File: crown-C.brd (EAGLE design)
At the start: 302 x 51.5 mm, 15 parts

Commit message: Mostly routed! :D
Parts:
- added U$1, U$3, U$4, U$5, U$6, U$7, U$8, U$9: SMD_BREADBOARD, pcb_crown:SMD_BREADBOARD_4X
- added U$10, U$11, U$12, U$13, U$14, U$15, U$16, U$17, U$18, U$19, U$20, U$21, U$22, U$23, U$24, U$25, U$26, U$27, U$28, U$29, U$30, U$31, U$32, U$33, U$34, U$35, U$36, U$37, U$38, U$39, U$40, U$41, U$42, U$43, U$44, U$45, U$46, U$47, U$48, U$49, U$50, U$51, U$52, U$53, U$54, U$55, U$56, U$57, U$58, U$59, U$60, U$61, U$62, U$63, U$64, U$65, U$66, U$67, U$68, U$69, U$70, U$71: SMD_PAD, pcb_crown:SMD_BREADBOARD_PAD
- moved SKIP-PTH1 10.0 mm to (19.6, 51.6), turned to 90 degrees
- moved C3 9.34 mm to (38.9, 53.8), turned to 270 degrees
- moved C4 9.24 mm to (19.8, 47.5), turned to 90 degrees
- moved SKIP-PTH2 4.64 mm to (49.3, 59.7)
- moved PTH1 0.13 mm to (14.5, 58.4)
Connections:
- net PTH-DI renamed PB1
- net SMD-DI renamed PB0
- new net A0: U$2.P$13, U$2.P$32, U$44.P$1, U$55.P$1
- new net A1: U$2.P$14, U$2.P$33, U$43.P$1, U$56.P$1
- new net A2: U$2.P$15, U$2.P$34, U$42.P$1, U$58.P$1
- new net N$11: U$14.P$1, U$15.P$1, U$5.P$3, U$57.P$1
- new net N$12: U$12.P$1, U$13.P$1, U$50.P$1, U$6.P$3
- new net N$13: U$10.P$1, U$11.P$1, U$49.P$1, U$7.P$3
- new net N$14: U$40.P$1, U$41.P$1, U$7.P$7, U$71.P$1
- new net N$15: U$38.P$1, U$39.P$1, U$6.P$7, U$70.P$1
- new net N$16: U$36.P$1, U$37.P$1, U$5.P$7, U$69.P$1
- new net N$17: U$34.P$1, U$35.P$1, U$4.P$7, U$68.P$1
- new net N$18: U$32.P$1, U$33.P$1, U$67.P$1, U$8.P$7
- new net N$19: U$30.P$1, U$31.P$1, U$66.P$1, U$9.P$7
- new net N$2: U$1.P$3, U$24.P$1, U$25.P$1, U$63.P$1
- new net N$20: U$28.P$1, U$29.P$1, U$3.P$7, U$65.P$1
- new net N$21: U$1.P$7, U$26.P$1, U$27.P$1, U$64.P$1
- new net N$6: U$22.P$1, U$23.P$1, U$3.P$3, U$62.P$1
- new net N$7: U$20.P$1, U$21.P$1, U$61.P$1, U$9.P$3
- new net N$8: U$18.P$1, U$19.P$1, U$60.P$1, U$8.P$3
- new net N$9: U$16.P$1, U$17.P$1, U$4.P$3, U$59.P$1
- new net PB2: U$2.P$28, U$2.P$9, U$48.P$1, U$51.P$1
- new net PB3: U$2.P$10, U$2.P$29, U$47.P$1, U$52.P$1
- new net PB4: U$2.P$11, U$2.P$30, U$46.P$1, U$53.P$1
- new net PB5: U$2.P$12, U$2.P$31, U$45.P$1, U$54.P$1
- net GND: now also U$1.P$2, U$2.P$18, U$2.P$37, U$3.P$2, U$4.P$2, U$5.P$2, U$6.P$2, U$7.P$2, U$8.P$2, U$9.P$2
- net N$4: now also U$2.P$19
- net PTH-DO: now also U$2.P$38
- net VBAT: now also U$2.P$16, U$2.P$35
- net VLIVE: now also U$1.P$1, U$2.P$17, U$2.P$36, U$3.P$1, U$4.P$1, U$5.P$1, U$6.P$1, U$7.P$1, U$8.P$1, U$9.P$1
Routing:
- net A2: track 0.00 -> 111.5 mm
- net A1: track 0.00 -> 108.2 mm
- net A0: track 0.00 -> 103.5 mm
- net PB5: track 0.00 -> 102.3 mm
- net PB4: track 0.00 -> 99.6 mm
- net PB3: track 0.00 -> 96.8 mm
- net PB2: track 0.00 -> 93.7 mm
- net VBAT: track 109.0 -> 194.9 mm
- net VLIVE: track 179.6 -> 240.0 mm, vias 7 -> 5
- net GND: track 172.9 -> 217.8 mm, vias 7 -> 5
- net N$4: track 44.6 -> 66.6 mm
- net N$5: track 67.8 -> 47.4 mm
- net PTH-DO: track 48.9 -> 58.2 mm
- net N$9: track 0.00 -> 7.62 mm
- net N$8: track 0.00 -> 7.62 mm
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- added copper zone on layer 1, net GND
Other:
- board size 302 x 51.5 mm -> 117.3 x 51.5 mm
- board text added: "A0"
- board text added: "A1"
- board text added: "A2"
- board text added: "D10"
- board text added: "D11"
- board text added: "D12"
- board text added: "D13"
- board text added: "SPI"

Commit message: Just cleanup stuff
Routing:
- net VBAT: track 194.9 -> 261.3 mm, vias 1 -> 3
- net VLIVE: track 240.0 -> 290.4 mm, vias 5 -> 6
- net A2: track 111.5 -> 114.6 mm
- net GND: track 217.8 -> 215.3 mm
- net A1: track 108.2 -> 110.7 mm
- net A0: track 103.5 -> 105.5 mm
- net PB5: track 102.3 -> 103.9 mm
- net PB4: track 99.6 -> 100.6 mm
- net PB3: track 96.8 -> 97.3 mm
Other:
- board text added: "A4"
- board text added: "A5"
- board text added: "D3"
- board text added: "D4"
- board text added: "D5"
- board text added: "I2C"
- board text added: "RXI"
- board text added: "TXO"
- board text removed: "A0"
- board text removed: "A1"
- board text removed: "A2"
- board text removed: "D10"
- board text removed: "D11"
- board text removed: "D12"
- board text removed: "D13"
- board text removed: "SPI"

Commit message: tidied up a little bit
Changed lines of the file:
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@@
 <layer number="27" name="tValues" color="7" fill="1" visible="no" active="yes"/>
 <layer number="28" name="bValues" color="7" fill="1" visible="no" active="yes"/>
-<layer number="29" name="tStop" color="7" fill="3" visible="no" active="yes"/>
+<layer number="29" name="tStop" color="7" fill="3" visible="yes" active="yes"/>
 <layer number="30" name="bStop" color="7" fill="6" visible="no" active="yes"/>
 <layer number="31" name="tCream" color="7" fill="4" visible="no" active="yes"/>
@@
 <polygon width="0.2032" layer="1" isolate="0.254" orphans="yes">
 <vertex x="0.254" y="15.24"/>
-<vertex x="0" y="53.34"/>
-<vertex x="7.62" y="67.31"/>
-<vertex x="17.272" y="67.056"/>
-<vertex x="19.558" y="74.93"/>
-<vertex x="38.1" y="74.93"/>
-<vertex x="40.64" y="67.31"/>
-<vertex x="51.054" y="67.31"/>
-<vertex x="51.054" y="58.166"/>
+<vertex x="0.254" y="50.8"/>
+<vertex x="9.906" y="58.42"/>
+<vertex x="18.796" y="58.674"/>
+<vertex x="26.67" y="50.8"/>
+<vertex x="34.544" y="55.88"/>
+<vertex x="39.37" y="66.294"/>
+<vertex x="48.26" y="66.294"/>
+<vertex x="50.292" y="58.166"/>
+<vertex x="54.102" y="52.578"/>
 <vertex x="58.42" y="50.8"/>
 <vertex x="58.42" y="15.24"/>

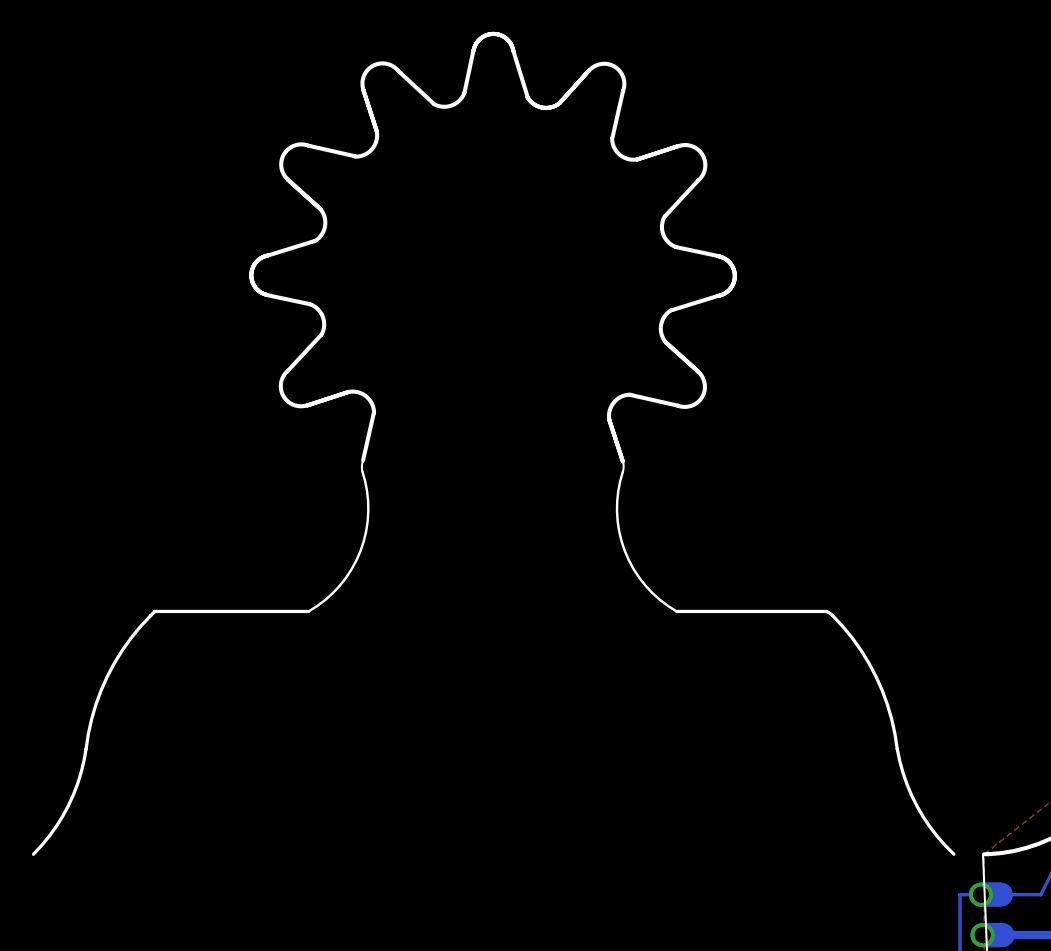
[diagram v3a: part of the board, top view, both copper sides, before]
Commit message: fixed dimension layer
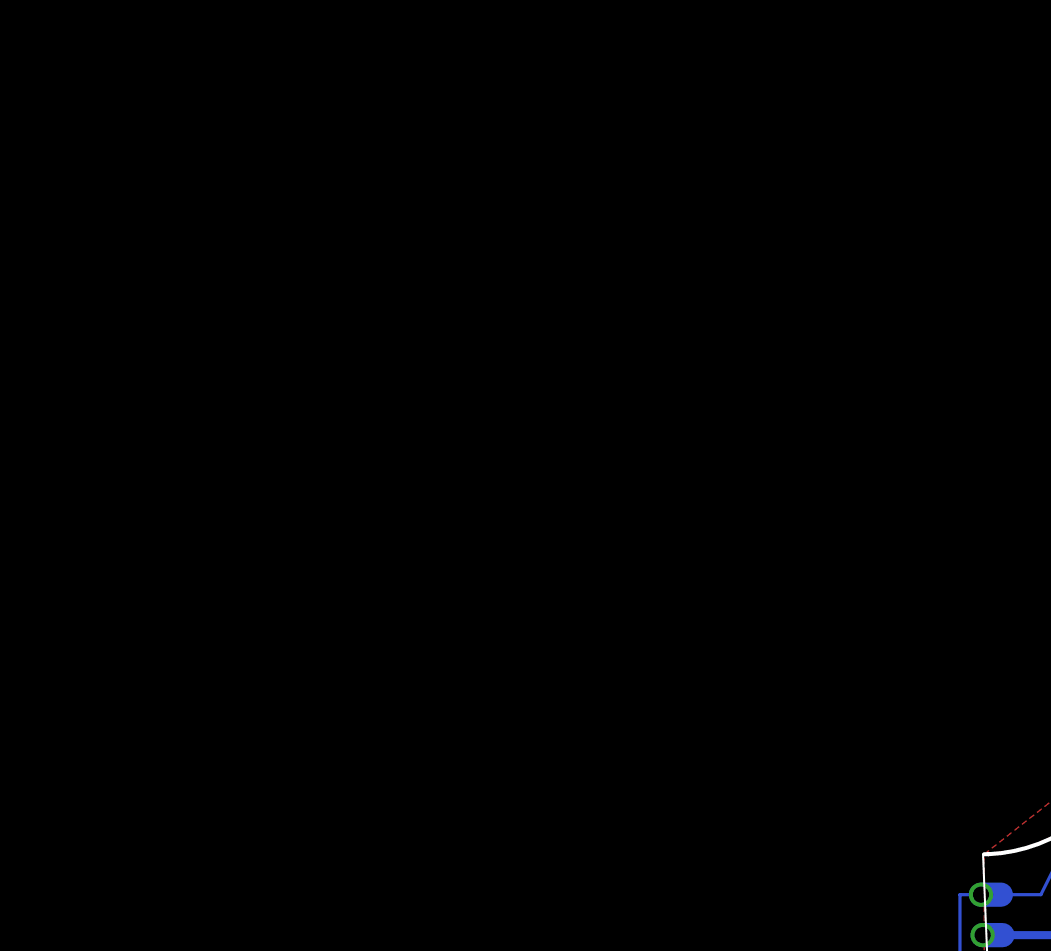
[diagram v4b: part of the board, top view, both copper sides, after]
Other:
- board size 117.3 x 51.5 mm -> 57.8 x 50.8 mm
